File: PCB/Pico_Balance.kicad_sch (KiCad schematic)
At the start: 13 parts, among them Q1 NMOS, U1 BMI160, U2 DRV8876PWPR, U3 DRV8876PWPR, U4 LM74610QDGKRQ1, U5 LMR51430

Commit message: Power and IMU Layout
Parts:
- added C4, C5: C, symbol Device:C
- added C6, C7: 100n, symbol Device:C
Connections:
- net +3V3: now reaches U1.1 (SDO)
- net +3V3: now also A1.36 (3V3), U1.12 (CSB), U1.5 (VDDIO), U1.8 (VDD), C6.1, C7.1
- net SCL: now reaches U1.13 (SCx)
- net SDA: now reaches U1.14 (SDx)
- net GND: now reaches U1.6 (GNDIO)
- net GND: now also A1.13 (GND), A1.18 (GND), A1.23 (GND), A1.28 (GND), A1.3 (GND), A1.33 (AGND), A1.38 (GND), A1.8 (GND), C2.2, R2.2, U1.7 (GND), U5.1 (GND), C4.2, C5.2, C6.2, C7.2
- net VM: now reaches C2.1, Q1.3 (S), U4.8 (CATHODE), U5.3 (VIN), U5.5 (EN)
- net VM: now also C4.1
- net +5V: now reaches L1.2, R1.1
- net +5V: now also A1.39 (VSYS), C5.1
- no-connect marks 2 -> 10
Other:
- moved on the sheet: A1, C2, C3, L1, R1, R2, U1, U5

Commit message: Initial Motor Drive Layout
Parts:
- added C8, C9: C, symbol Device:C
- added JP1: SolderJumper_3_Bridged12, Jumper:SolderJumper-3_P1.3mm_Bridged12_Pad1.0x1.5mm_NumberLabels, symbol Jumper:SolderJumper_3_Bridged12
- added R3, R4: R, symbol Device:R
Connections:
- net +3V3: now also U2.5 (VREF), JP1.1 (A), R3.1
- net GND: now also U2.15 (GND), U2.17 (PAD), U2.7 (IMODE), U2.9 (PGND), U3.15 (GND), U3.17 (PAD), U3.9 (PGND), JP1.3 (B), R4.1
- net VM: now also U2.11 (VM), U3.11 (VM), C9.1
- net IN1: now reaches U2.1 (EN_IN1)
- net at U2.12 (VCP): now also C9.2
- net at U2.13 (CPH): now also C8.1
- net at U2.14 (CPL): now also C8.2
- net at U2.16 (PMODE): now also JP1.2 (C)
- net IN2: now reaches U2.2 (PH_IN2)
- net SLP0: now reaches U2.3 (SLEEP_N)
- net at U2.4 (FAULT_N): now also R3.2
- net CS0: now reaches U2.6 (IPROPI)
- net CS0: now also R4.2
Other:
- moved on the sheet: U2

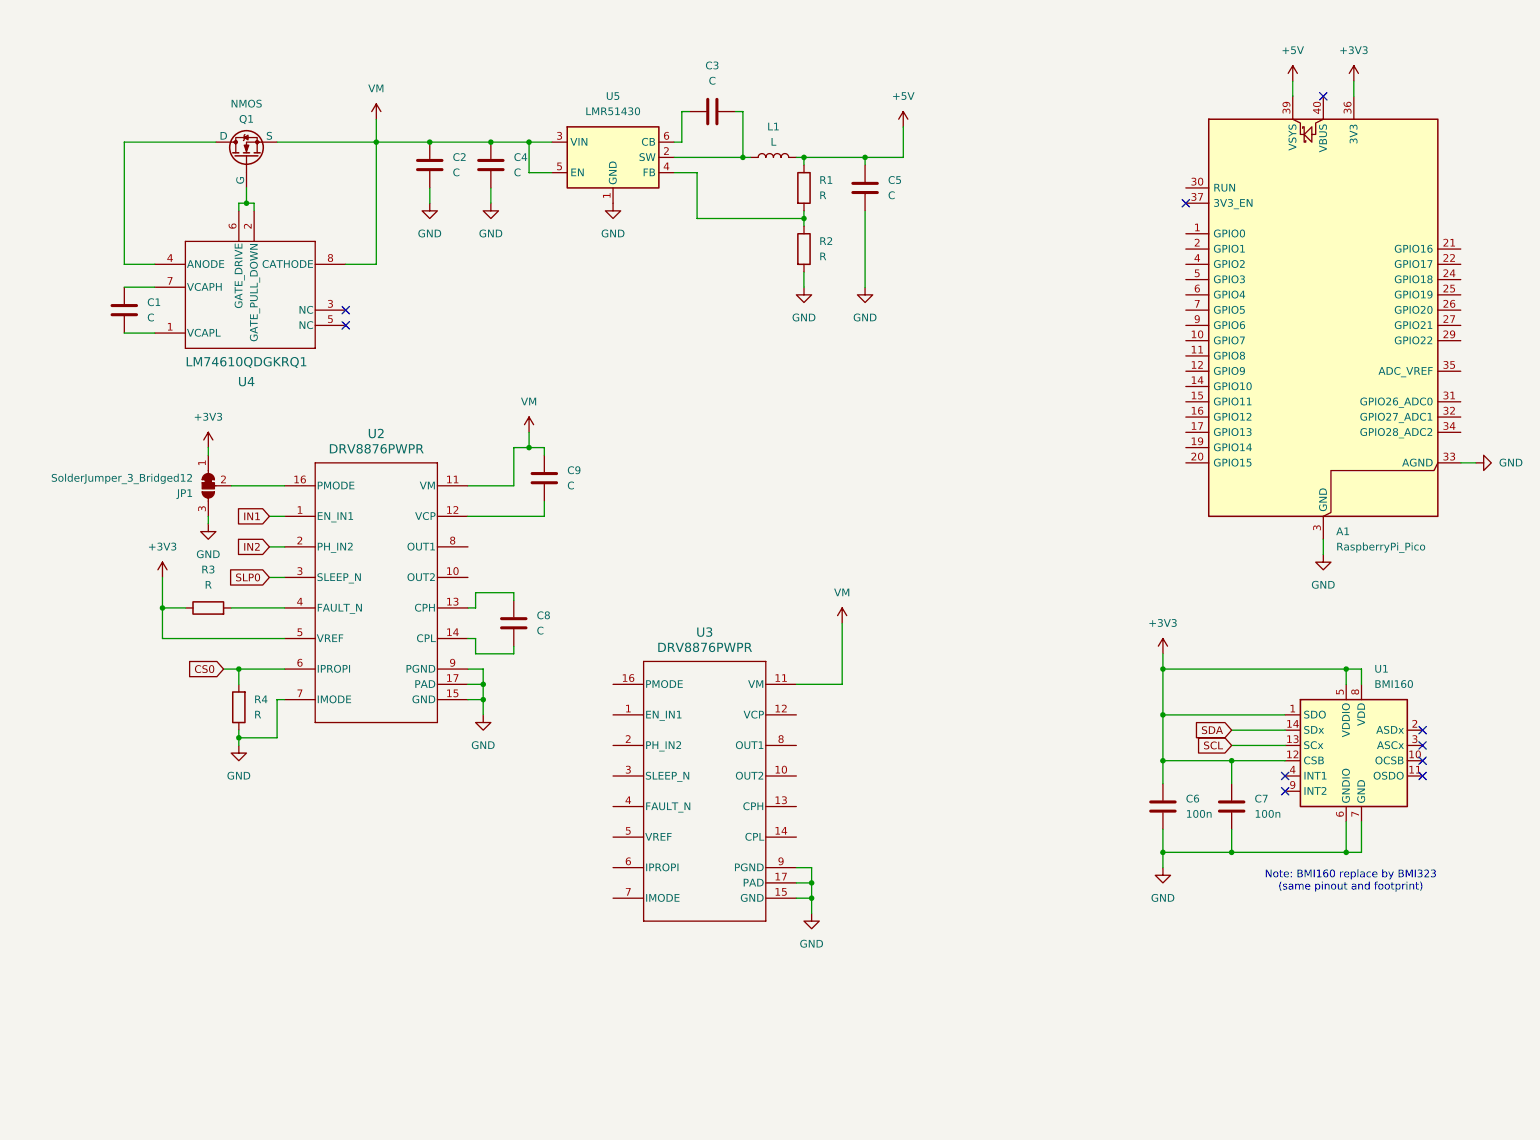
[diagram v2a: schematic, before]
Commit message: Most component values assigned
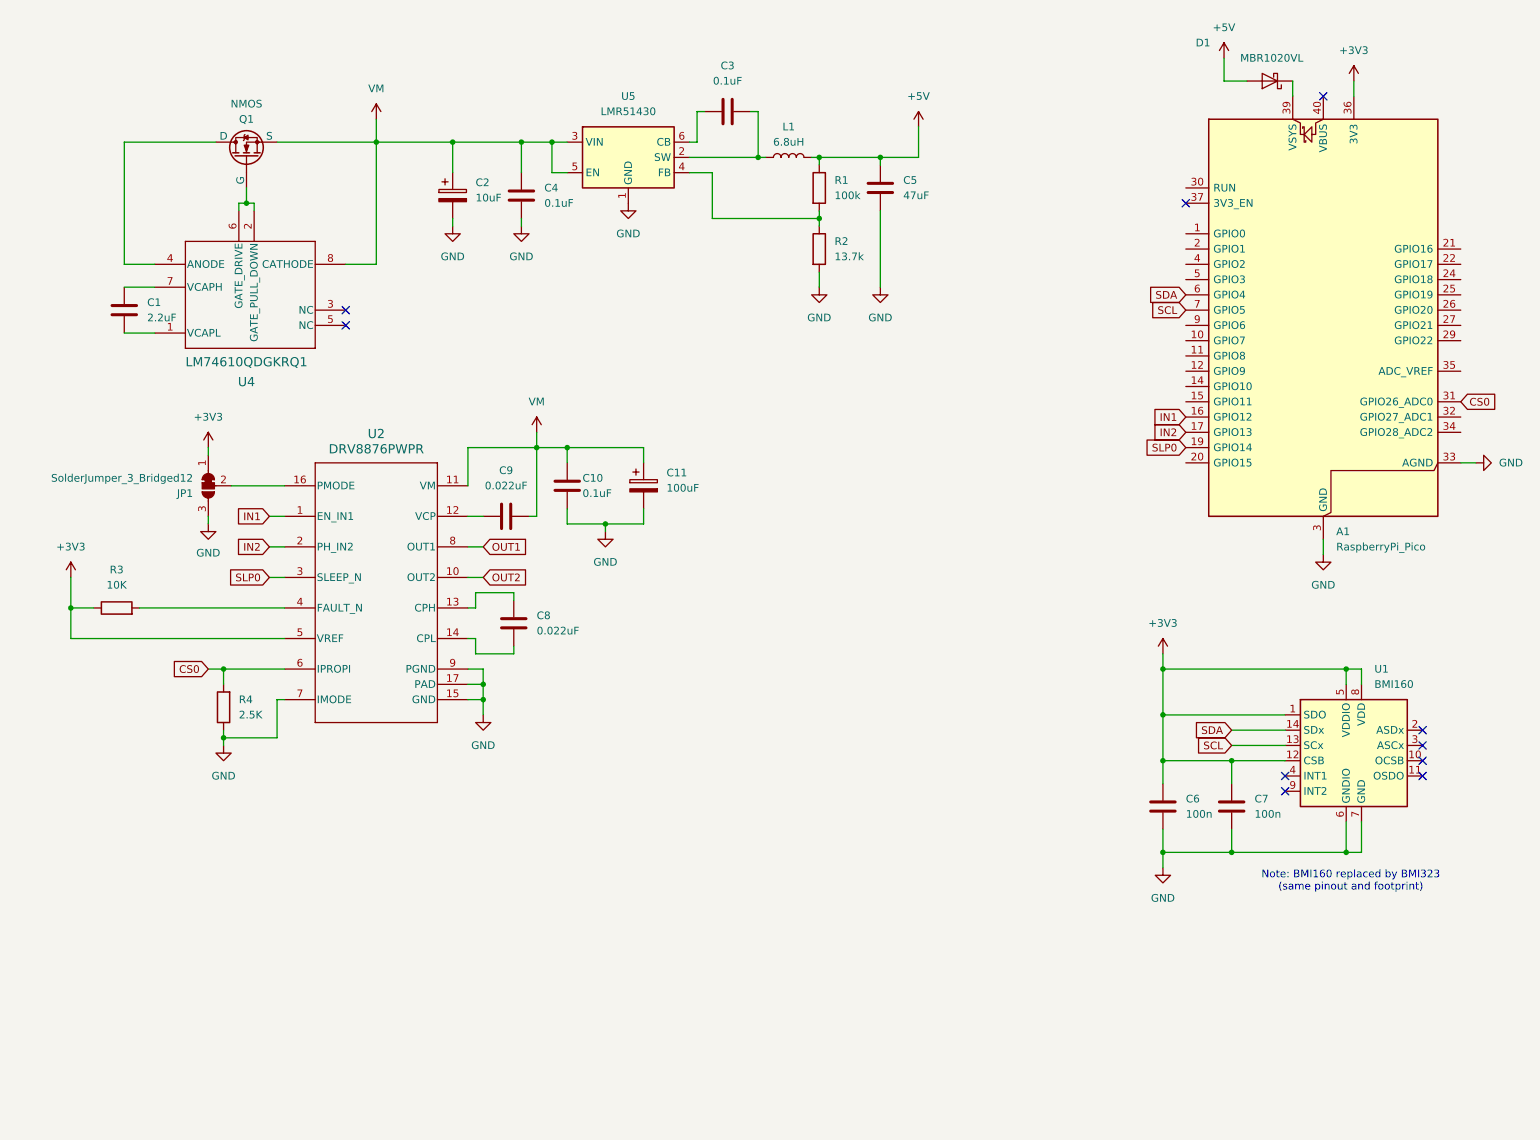
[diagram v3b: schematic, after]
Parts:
- removed C2: C, symbol Device:C
- removed U3: DRV8876PWPR, PWP0016J_N, symbol 2025-06-21_13-03-58:DRV8876PWPR
- added C10: 0.1uF, symbol Device:C
- added C11: 100uF, symbol Device:C_Polarized
- added C2: 10uF, symbol Device:C_Polarized
- added D1: MBR1020VL, Diode_SMD:D_SOD-123F, symbol Diode:MBR1020VL
- C1: value C -> 2.2uF
- C3, C4: value C -> 0.1uF
- C5: value C -> 47uF
- C8, C9: value C -> 0.022uF
- L1: value L -> 6.8uH
- R1: value R -> 100k
- R2: value R -> 13.7k
- R3: value R -> 10K
- R4: value R -> 2.5K
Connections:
- net +5V: now also D1.2 (A); no longer A1.39 (VSYS)
- net CS0: now also A1.31 (GPIO26_ADC0)
- net GND: now also C10.2, C11.2, C2.2
- net IN1: now also A1.16 (GPIO12)
- net IN2: now also A1.17 (GPIO13)
- net SCL: now also A1.7 (GPIO5)
- net SDA: now also A1.6 (GPIO4)
- net SLP0: now also A1.19 (GPIO14)
- net VM: now also C9.2, C10.1, C11.1, C2.1; no longer C9.1
- net at U2.12 (VCP): now also C9.1; no longer C9.2
- net OUT2: now reaches U2.10 (OUT2)
- net OUT1: now reaches U2.8 (OUT1)
- new net: A1.39 (VSYS), D1.1 (K)
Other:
- note added: "Note: BMI160 replaced by BMI323 (same pinout and footprint)"
- note removed: "Note: BMI160 replace by BMI323 (same pinout and footprint)"
- moved on the sheet: C3, C4, C5, C9, L1, R1, R2, R3, R4, U5

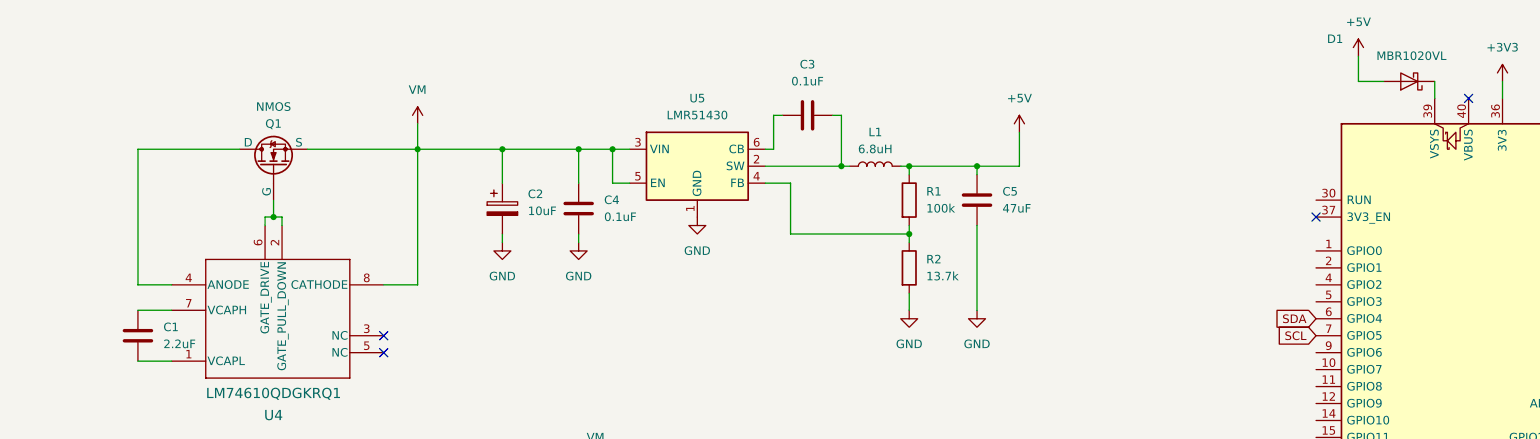
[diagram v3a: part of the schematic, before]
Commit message: Add TVS Diode
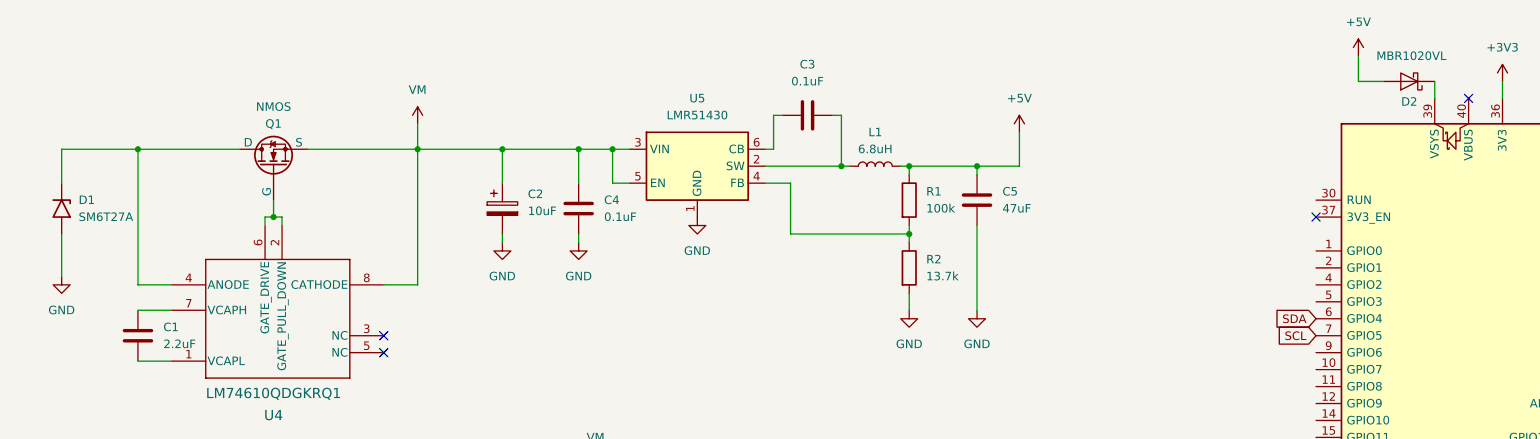
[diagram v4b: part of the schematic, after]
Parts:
- added D1: SM6T27A, LED_SMD:LED-L1T2_LUMILEDS, symbol Diode:SM6T27A
- renumbered D1 to D2
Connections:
- net GND: now also D1.2 (A2)
- net at Q1.1 (D), U4.4 (ANODE): now also D1.1 (A1)
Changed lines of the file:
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@@
 	)
 	(junction
+		(at 29.21 34.29)
+		(diameter 0)
+		(color 0 0 0 0)
+	)
+	(junction
 		(at 201.93 121.92)
 		(diameter 0)
@@
 	(wire
 		(pts
+			(xy 17.78 34.29) (xy 29.21 34.29)
+		)
+		(stroke
+			(width 0)
+			(type default)
+		)
+	)
+	(wire
+		(pts
 			(xy 124.46 29.21) (xy 124.46 34.29)
 		)
@@
 	(wire
 		(pts
+			(xy 17.78 46.99) (xy 17.78 53.34)
+		)
+		(stroke
+			(width 0)
+			(type default)
+		)
+	)
+	(wire
+		(pts
 			(xy 144.78 36.83) (xy 144.78 38.1)
 		)
@@
 	(wire
 		(pts
+			(xy 17.78 39.37) (xy 17.78 34.29)
+		)
+		(stroke
+			(width 0)
+			(type default)
+		)
+	)
+	(wire
+		(pts
 			(xy 55.88 121.92) (xy 45.72 121.92)
 		)
@@
 	)
 	(symbol
+		(lib_id "power:GND")
+		(at 17.78 53.34 0)
+		(unit 1)
+		(exclude_from_sim no)
+		(in_bom yes)
+		(on_board yes)
+		(dnp no)
+		(fields_autoplaced yes)
+		(property "Reference" "#PWR015"
+			(at 17.78 59.69 0)
+			(effects
+				(font
+					(size 1.27 1.27)
+				)
+				(hide yes)
+			)
+		)
+		(property "Value" "GND"
+			(at 17.78 58.42 0)
+			(effects
+				(font
+					(size 1.27 1.27)
+				)
+			)
+		)
+		(property "Footprint" ""
+			(at 17.78 53.34 0)
+			(effects
+				(font
+					(size 1.27 1.27)
+				)
+				(hide yes)
+			)
+		)
+		(property "Datasheet" ""
+			(at 17.78 53.34 0)
+			(effects
+				(font
+					(size 1.27 1.27)
+				)
+				(hide yes)
+			)
+		)
+		(property "Description" "Power symbol creates a global label with name \"GND\" , ground"
+			(at 17.78 53.34 0)
+			(effects
+				(font
+					(size 1.27 1.27)
+				)
+				(hide yes)
+			)
+		)
+		(pin "1"
+		)
+		(instances
+			(project ""
+				(path "/07906831-fbcb-4dc7-83a6-3d3bd7082898"
+					(reference "#PWR015")
+					(unit 1)
+				)
+			)
+		)
+	)
+	(symbol
 		(lib_id "Jumper:SolderJumper_3_Bridged12")
 		(at 43.18 91.44 90)
@@
 		(on_board yes)
 		(dnp no)
-		(property "Reference" "D1"
-			(at 208.5975 17.78 0)
+		(property "Reference" "D2"
+			(at 219.71 27.178 0)
 			(effects
 				(font
@@
 			(project ""
 				(path "/07906831-fbcb-4dc7-83a6-3d3bd7082898"
-					(reference "D1")
+					(reference "D2")
 					(unit 1)
 				)
@@
 					(unit 1)
 				)
+			)
+		)
+	)
+	(symbol
+		(lib_id "Diode:SM6T27A")
+		(at 17.78 43.18 270)
+		(unit 1)
+		(exclude_from_sim no)
+		(in_bom yes)
+		(on_board yes)
+		(dnp no)
+		(fields_autoplaced yes)
+		(property "Reference" "D1"
+			(at 20.32 41.9099 90)
+			(effects
+				(font
+					(size 1.27 1.27)
+				)
+				(justify left)
+			)
+		)
+		(property "Value" "SM6T27A"
+			(at 20.32 44.4499 90)
+			(effects
+				(font
+					(size 1.27 1.27)
+				)
+				(justify left)
+			)
+		)
+		(property "Footprint" "LED_SMD:LED-L1T2_LUMILEDS"
+			(at 12.7 43.18 0)
+			(effects
+				(font
+					(size 1.27 1.27)
+				)
+				(hide yes)
+			)
+		)
+		(property "Datasheet" "https://www.st.com/resource/en/datasheet/sm6t.pdf"
+			(at 17.78 41.91 0)
+			(effects
+				(font
+					(size 1.27 1.27)
+				)
+				(hide yes)
+			)
+		)
+		(property "Description" "600W unidirectional Transil Transient Voltage Suppressor, 27Vrwm, DO-214AA"
+			(at 17.78 43.18 0)
+			(effects
+				(font
+					(size 1.27 1.27)
+				)
+				(hide yes)
+			)
+		)
+		(pin "1"
+		)
+		(pin "2"
+		)
+		(instances
+			(project ""
+				(path "/07906831-fbcb-4dc7-83a6-3d3bd7082898"
+					(reference "D1")
+					(unit 1)
+				)
